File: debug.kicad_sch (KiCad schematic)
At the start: 2 parts, among them J6 Conn_ARM_JTAG_SWD_10, J7 Conn_01x03

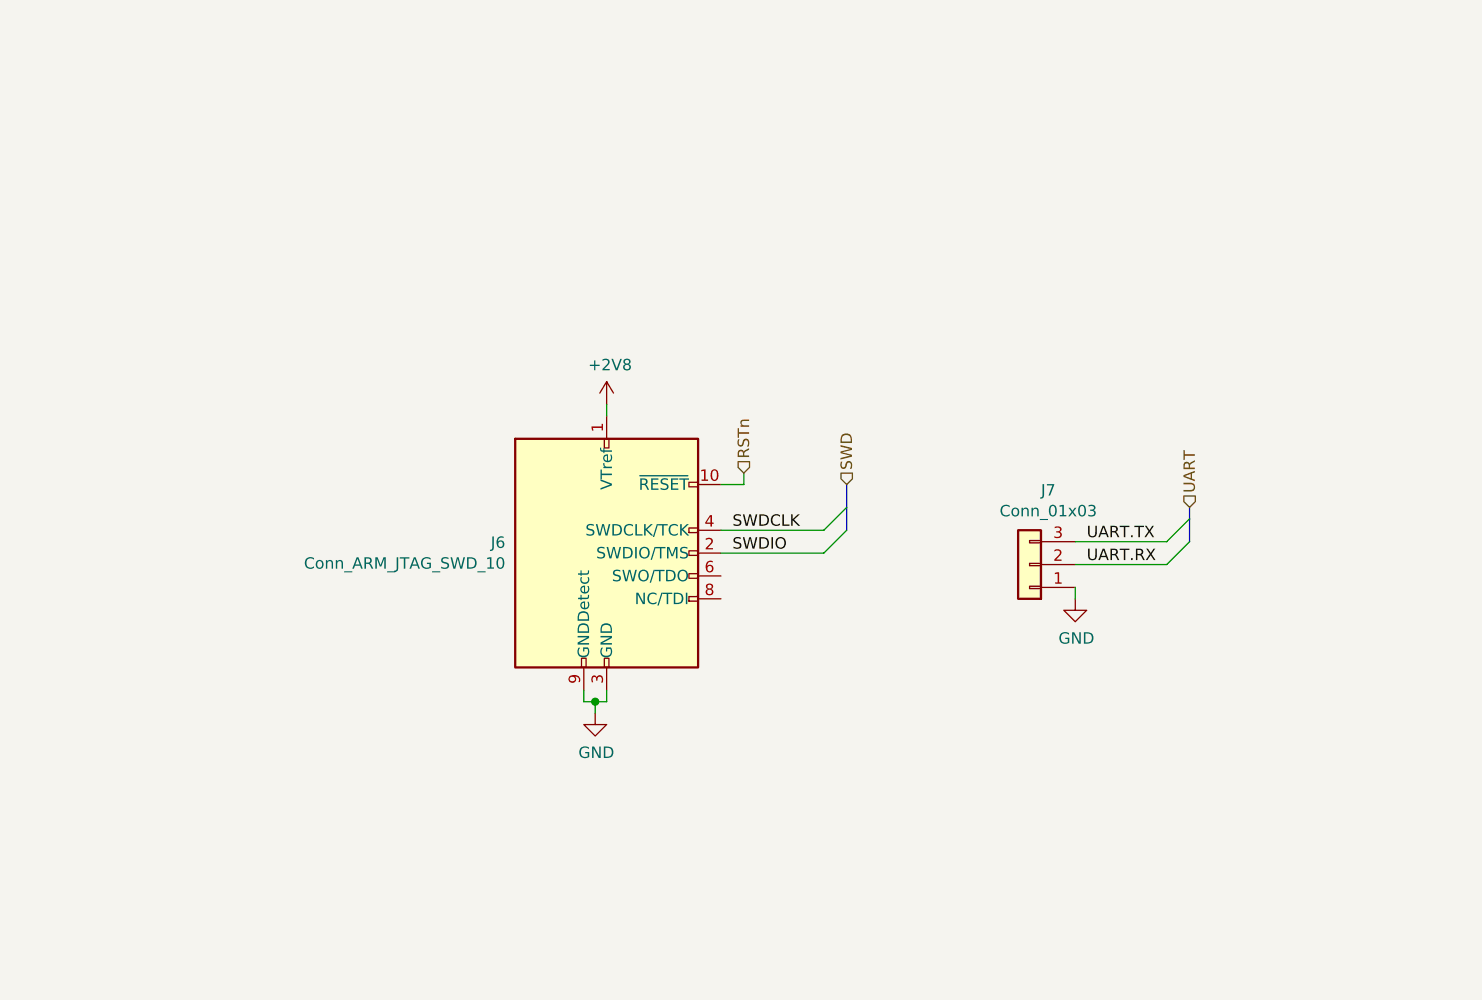
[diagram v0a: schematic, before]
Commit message: Initial schematic version
This is now a clean and ready version of the schematic:
That means:
- Schematic has been reviewed,
- It's fully annotated,
- All elements have been checked for availability with JLCPCB,
- Footprints were assigned,
- ERC is green.

No design changes should be added for this version until
the PCB is present and version is released.
Only bugfixes are possible now.
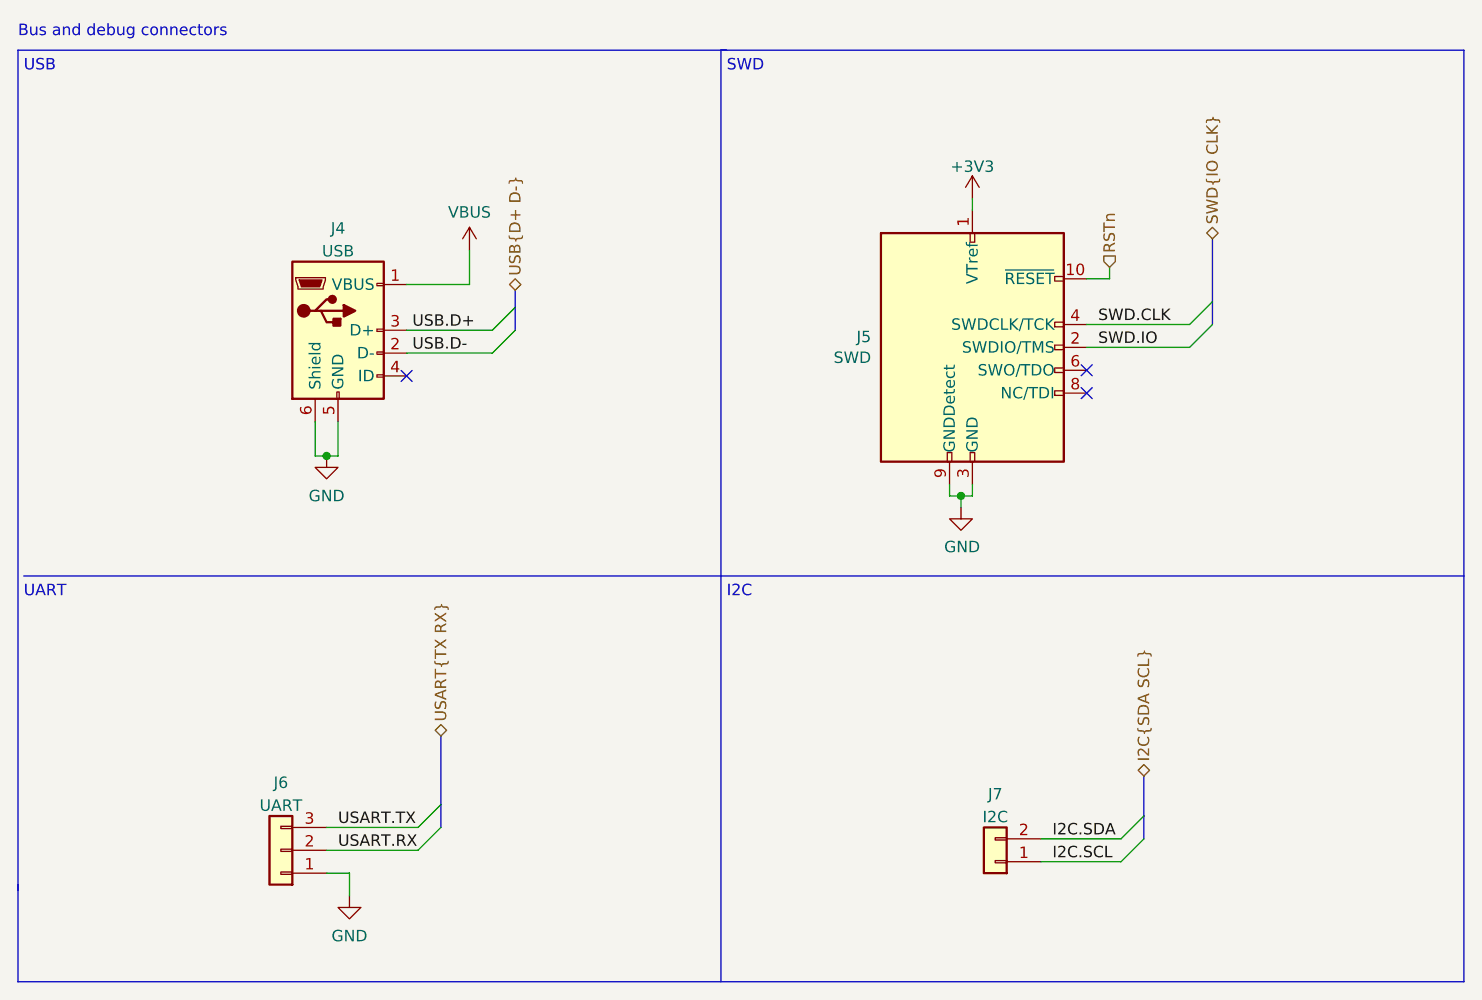
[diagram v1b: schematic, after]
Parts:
- removed J7: Conn_01x03, Connector_PinHeader_2.54mm:PinHeader_1x03_P2.54mm_Vertical, symbol Connector_Generic:Conn_01x03
- added J4: USB, Connector_USB:USB_Micro-B_Molex-105017-0001, symbol Connector:USB_B_Micro
- added J6: UART, Connector_PinHeader_2.54mm:PinHeader_1x03_P2.54mm_Vertical, symbol Connector_Generic:Conn_01x03
- added J7: I2C, Connector_PinHeader_2.54mm:PinHeader_1x02_P2.54mm_Vertical, symbol Connector_Generic:Conn_01x02
- J5: renamed from J6; value Conn_ARM_JTAG_SWD_10 -> SWD
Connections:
- net GND: now also J4.5 (GND), J4.6 (Shield), J6.1 (Pin_1)
- net +2V8 renamed +3V3
- net SWDCLK renamed SWD.CLK
- net SWDIO renamed SWD.IO
- new net I2C.SCL: J7.1 (Pin_1)
- new net I2C.SDA: J7.2 (Pin_2)
- new net USART.RX: J6.2 (Pin_2)
- new net USART.TX: J6.3 (Pin_3)
- new net USB.D+: J4.3 (D+)
- new net USB.D-: J4.2 (D-)
- new net VBUS: J4.1 (VBUS)
- no-connect marks 0 -> 3
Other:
- note added: "Bus and debug connectors"
- note added: "I2C"
- note added: "SWD"
- note added: "UART"
- note added: "USB"
- moved on the sheet: J5

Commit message: Update footprints and add JLCPCB fields
Update some footprints which will suit better building the pcb
with JLCBPCB. Add fields to components sourced from JLCPCB
to be able to generate BOM.
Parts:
- J4: JLC (none) -> SMD; LCSC (none) -> C136000
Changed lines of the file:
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@@
+      (effects (font (size 1.27 1.27)) hide)
+    )
+    (property "JLC" "SMD" (id 4) (at 94.615 70.485 0)
+      (effects (font (size 1.27 1.27)) hide)
+    )
+    (property "LCSC" "C136000" (id 5) (at 94.615 70.485 0)
       (effects (font (size 1.27 1.27)) hide)
     )
